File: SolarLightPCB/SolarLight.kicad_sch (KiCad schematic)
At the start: 20 parts, among them J1 I2C, J2 SPI, U1 TP4056, U2 WeMos_D1_mini, U3 MCP1700-3302E

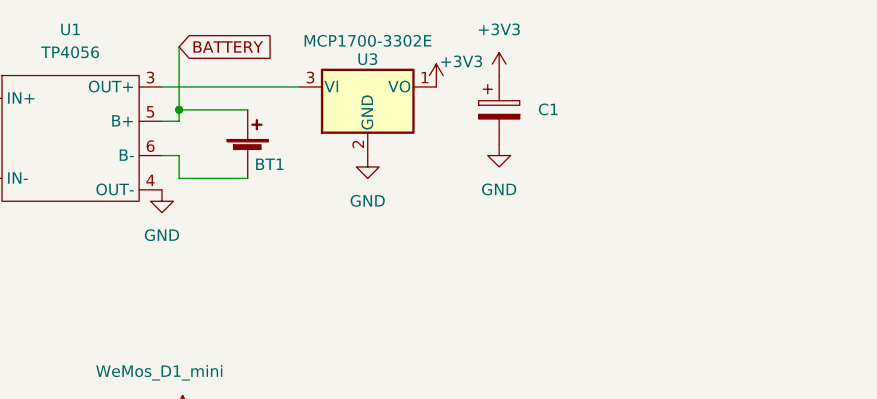
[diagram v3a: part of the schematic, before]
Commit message: Add a power on Jumper
fixes #5
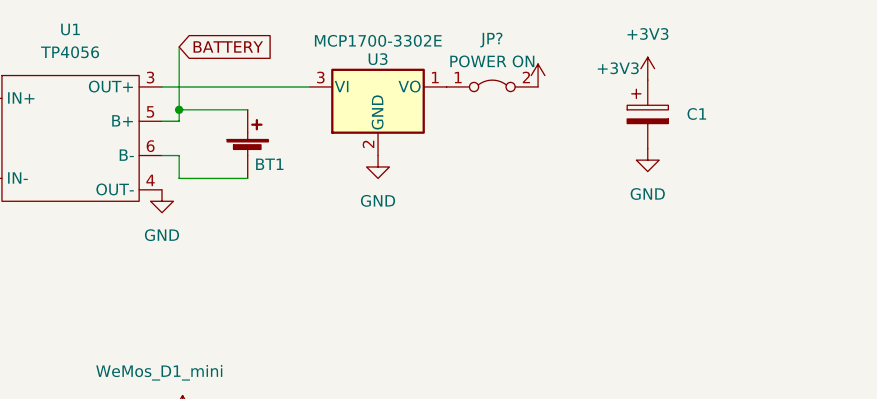
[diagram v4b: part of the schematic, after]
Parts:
- added JP?: POWER ON, Connector_PinHeader_2.54mm:PinHeader_1x02_P2.54mm_Vertical, symbol Jumper:Jumper_2_Bridged
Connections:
- net +3V3: now also JP?.2 (B); no longer U3.1 (VO)
- new net: JP?.1 (A), U3.1 (VO)
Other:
- moved on the sheet: C1, U3
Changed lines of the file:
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@@
     (stroke (width 0) (type default) (color 0 0 0 0))
   )
-  (wire (pts (xy 138.811 39.624) (xy 154.051 39.624))
+  (wire (pts (xy 138.811 39.624) (xy 155.194 39.624))
     (stroke (width 0) (type default) (color 0 0 0 0))
   )
@@
     (pin "2")
   )
-  (symbol (lib_id "power:GND") (at 176.276 45.974 0) (unit 1)
-    (in_bom yes) (on_board yes) (fields_autoplaced)
-    (property "Reference" "#PWR0103" (id 0) (at 176.276 52.324 0)
-      (effects (font (size 1.27 1.27)) hide)
-    )
-    (property "Value" "GND" (id 1) (at 176.276 51.054 0))
-    (property "Footprint" "" (id 2) (at 176.276 45.974 0)
-      (effects (font (size 1.27 1.27)) hide)
-    )
-    (property "Datasheet" "" (id 3) (at 176.276 45.974 0)
+  (symbol (lib_id "power:GND") (at 192.786 46.482 0) (unit 1)
+    (in_bom yes) (on_board yes) (fields_autoplaced)
+    (property "Reference" "#PWR0103" (id 0) (at 192.786 52.832 0)
+      (effects (font (size 1.27 1.27)) hide)
+    )
+    (property "Value" "GND" (id 1) (at 192.786 51.562 0))
+    (property "Footprint" "" (id 2) (at 192.786 46.482 0)
+      (effects (font (size 1.27 1.27)) hide)
+    )
+    (property "Datasheet" "" (id 3) (at 192.786 46.482 0)
       (effects (font (size 1.27 1.27)) hide)
     )
@@
     (pin "1")
   )
-  (symbol (lib_id "power:+3V3") (at 169.291 39.624 0) (unit 1)
-    (in_bom yes) (on_board yes)
-    (property "Reference" "#PWR0104" (id 0) (at 169.291 43.434 0)
-      (effects (font (size 1.27 1.27)) hide)
-    )
-    (property "Value" "+3V3" (id 1) (at 172.085 36.83 0))
-    (property "Footprint" "" (id 2) (at 169.291 39.624 0)
-      (effects (font (size 1.27 1.27)) hide)
-    )
-    (property "Datasheet" "" (id 3) (at 169.291 39.624 0)
+  (symbol (lib_id "power:+3V3") (at 180.594 39.624 0) (unit 1)
+    (in_bom yes) (on_board yes)
+    (property "Reference" "#PWR0104" (id 0) (at 180.594 43.434 0)
+      (effects (font (size 1.27 1.27)) hide)
+    )
+    (property "Value" "+3V3" (id 1) (at 189.484 37.592 0))
+    (property "Footprint" "" (id 2) (at 180.594 39.624 0)
+      (effects (font (size 1.27 1.27)) hide)
+    )
+    (property "Datasheet" "" (id 3) (at 180.594 39.624 0)
       (effects (font (size 1.27 1.27)) hide)
     )
@@
     )
   )
-  (symbol (lib_id "Regulator_Linear:L78L33_TO92") (at 161.671 39.624 0) (unit 1)
-    (in_bom yes) (on_board yes)
-    (property "Reference" "U3" (id 0) (at 161.671 36.576 0))
-    (property "Value" "MCP1700-3302E" (id 1) (at 161.671 34.544 0))
-    (property "Footprint" "Package_TO_SOT_THT:TO-92_Inline" (id 2) (at 161.671 33.909 0)
+  (symbol (lib_id "Regulator_Linear:L78L33_TO92") (at 162.814 39.624 0) (unit 1)
+    (in_bom yes) (on_board yes)
+    (property "Reference" "U3" (id 0) (at 162.814 36.576 0))
+    (property "Value" "MCP1700-3302E" (id 1) (at 162.814 34.544 0))
+    (property "Footprint" "Package_TO_SOT_THT:TO-92_Inline" (id 2) (at 162.814 33.909 0)
       (effects (font (size 1.27 1.27) italic) hide)
     )
-    (property "Datasheet" "http://www.st.com/content/ccc/resource/technical/document/datasheet/15/55/e5/aa/23/5b/43/fd/CD00000446.pdf/files/CD00000446.pdf/jcr:content/translations/en.CD00000446.pdf" (id 3) (at 161.671 40.894 0)
+    (property "Datasheet" "http://www.st.com/content/ccc/resource/technical/document/datasheet/15/55/e5/aa/23/5b/43/fd/CD00000446.pdf/files/CD00000446.pdf/jcr:content/translations/en.CD00000446.pdf" (id 3) (at 162.814 40.894 0)
       (effects (font (size 1.27 1.27)) hide)
     )
@@
     (pin "2")
   )
-  (symbol (lib_id "power:+3V3") (at 176.276 38.354 0) (unit 1)
-    (in_bom yes) (on_board yes) (fields_autoplaced)
-    (property "Reference" "#PWR0105" (id 0) (at 176.276 42.164 0)
-      (effects (font (size 1.27 1.27)) hide)
-    )
-    (property "Value" "+3V3" (id 1) (at 176.276 33.274 0))
-    (property "Footprint" "" (id 2) (at 176.276 38.354 0)
-      (effects (font (size 1.27 1.27)) hide)
-    )
-    (property "Datasheet" "" (id 3) (at 176.276 38.354 0)
+  (symbol (lib_id "power:+3V3") (at 192.786 38.862 0) (unit 1)
+    (in_bom yes) (on_board yes) (fields_autoplaced)
+    (property "Reference" "#PWR0105" (id 0) (at 192.786 42.672 0)
+      (effects (font (size 1.27 1.27)) hide)
+    )
+    (property "Value" "+3V3" (id 1) (at 192.786 33.782 0))
+    (property "Footprint" "" (id 2) (at 192.786 38.862 0)
+      (effects (font (size 1.27 1.27)) hide)
+    )
+    (property "Datasheet" "" (id 3) (at 192.786 38.862 0)
       (effects (font (size 1.27 1.27)) hide)
     )
@@
     )
   )
+  (symbol (lib_id "Jumper:Jumper_2_Bridged") (at 175.514 39.624 0) (unit 1)
+    (in_bom yes) (on_board yes) (fields_autoplaced)
+    (property "Reference" "JP?" (id 0) (at 175.514 34.29 0))
+    (property "Value" "POWER ON" (id 1) (at 175.514 36.83 0))
+    (property "Footprint" "Connector_PinHeader_2.54mm:PinHeader_1x02_P2.54mm_Vertical" (id 2) (at 175.514 39.624 0)
+      (effects (font (size 1.27 1.27)) hide)
+    )
+    (property "Datasheet" "~" (id 3) (at 175.514 39.624 0)
+      (effects (font (size 1.27 1.27)) hide)
+    )
+    (pin "1")
+    (pin "2")
+  )
   (symbol (lib_id "Connector:Conn_01x04_Female") (at 190.119 83.947 0) (unit 1)
     (in_bom yes) (on_board yes) (fields_autoplaced)
@@
     (pin "4")
   )
-  (symbol (lib_id "power:GND") (at 161.671 47.244 0) (unit 1)
-    (in_bom yes) (on_board yes) (fields_autoplaced)
-    (property "Reference" "#PWR0102" (id 0) (at 161.671 53.594 0)
-      (effects (font (size 1.27 1.27)) hide)
-    )
-    (property "Value" "GND" (id 1) (at 161.671 52.324 0))
-    (property "Footprint" "" (id 2) (at 161.671 47.244 0)
-      (effects (font (size 1.27 1.27)) hide)
-    )
-    (property "Datasheet" "" (id 3) (at 161.671 47.244 0)
+  (symbol (lib_id "power:GND") (at 162.814 47.244 0) (unit 1)
+    (in_bom yes) (on_board yes) (fields_autoplaced)
+    (property "Reference" "#PWR0102" (id 0) (at 162.814 53.594 0)
+      (effects (font (size 1.27 1.27)) hide)
+    )
+    (property "Value" "GND" (id 1) (at 162.814 52.324 0))
+    (property "Footprint" "" (id 2) (at 162.814 47.244 0)
+      (effects (font (size 1.27 1.27)) hide)
+    )
+    (property "Datasheet" "" (id 3) (at 162.814 47.244 0)
       (effects (font (size 1.27 1.27)) hide)
     )
@@
     (pin "3")
   )
-  (symbol (lib_id "Device:C_Polarized") (at 176.276 42.164 0) (unit 1)
-    (in_bom yes) (on_board yes)
-    (property "Reference" "C1" (id 0) (at 180.594 42.164 0)
-      (effects (font (size 1.27 1.27)) (justify left))
-    )
-    (property "Value" "C_Polarized" (id 1) (at 180.086 42.5449 0)
-      (effects (font (size 1.27 1.27)) (justify left) hide)
-    )
-    (property "Footprint" "Capacitor_THT:CP_Radial_D5.0mm_P2.00mm" (id 2) (at 177.2412 45.974 0)
-      (effects (font (size 1.27 1.27)) hide)
-    )
-    (property "Datasheet" "~" (id 3) (at 176.276 42.164 0)
+  (symbol (lib_id "Device:C_Polarized") (at 192.786 42.672 0) (unit 1)
+    (in_bom yes) (on_board yes)
+    (property "Reference" "C1" (id 0) (at 197.104 42.672 0)
+      (effects (font (size 1.27 1.27)) (justify left))
+    )
+    (property "Value" "C_Polarized" (id 1) (at 196.596 43.0529 0)
+      (effects (font (size 1.27 1.27)) (justify left) hide)
+    )
+    (property "Footprint" "Capacitor_THT:CP_Radial_D5.0mm_P2.00mm" (id 2) (at 193.7512 46.482 0)
+      (effects (font (size 1.27 1.27)) hide)
+    )
+    (property "Datasheet" "~" (id 3) (at 192.786 42.672 0)
       (effects (font (size 1.27 1.27)) hide)
     )
@@
       (reference "JP2") (unit 1) (value "Bridge") (footprint "Resistor_THT:R_Box_L8.4mm_W2.5mm_P5.08mm")
     )
+    (path "/a7c8a88d-781a-4fef-ada5-cbae7e10a79c"
+      (reference "JP?") (unit 1) (value "POWER ON") (footprint "Connector_PinHeader_2.54mm:PinHeader_1x02_P2.54mm_Vertical")
+    )
     (path "/efe1edb9-34c9-473f-839b-20e06ddf294c"

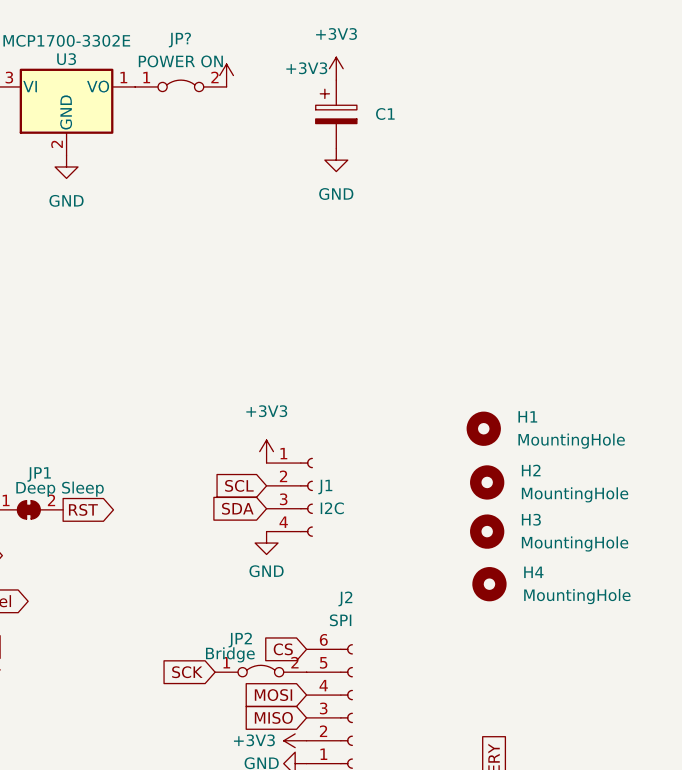
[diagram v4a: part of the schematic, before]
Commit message: Minor changes to PCB
- Added _draft_ mounting holes
- Added SPI and I2C labels
- Changed the Board dimension to 100x45mm
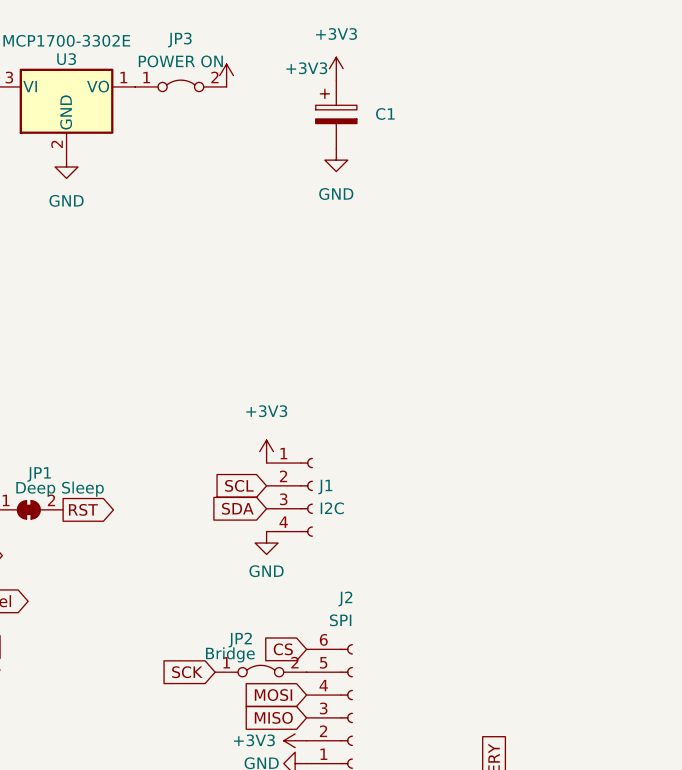
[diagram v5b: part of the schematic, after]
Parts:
- removed H1, H2, H3, H4: MountingHole, MountingHole:MountingHole_3.2mm_M3, symbol Mechanical:MountingHole
- U3: footprint Package_TO_SOT_THT:TO-92_Inline -> Package_TO_SOT_THT:TO-92
- gave numbers to parts that had none: 1
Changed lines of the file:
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@@
     (pin "1")
-  )
-  (symbol (lib_id "Mechanical:MountingHole") (at 209.169 77.597 0) (unit 1)
-    (in_bom yes) (on_board yes) (fields_autoplaced)
-    (property "Reference" "H1" (id 0) (at 212.852 76.3269 0)
-      (effects (font (size 1.27 1.27)) (justify left))
-    )
-    (property "Value" "MountingHole" (id 1) (at 212.852 78.8669 0)
-      (effects (font (size 1.27 1.27)) (justify left))
-    )
-    (property "Footprint" "MountingHole:MountingHole_3.2mm_M3" (id 2) (at 209.169 77.597 0)
-      (effects (font (size 1.27 1.27)) hide)
-    )
-    (property "Datasheet" "~" (id 3) (at 209.169 77.597 0)
-      (effects (font (size 1.27 1.27)) hide)
-    )
   )
   (symbol (lib_id "power:GND") (at 113.919 107.188 0) (unit 1)
@@
     (pin "1")
   )
-  (symbol (lib_id "Mechanical:MountingHole") (at 209.55 89.027 0) (unit 1)
-    (in_bom yes) (on_board yes) (fields_autoplaced)
-    (property "Reference" "H3" (id 0) (at 213.233 87.7569 0)
-      (effects (font (size 1.27 1.27)) (justify left))
-    )
-    (property "Value" "MountingHole" (id 1) (at 213.233 90.2969 0)
-      (effects (font (size 1.27 1.27)) (justify left))
-    )
-    (property "Footprint" "MountingHole:MountingHole_3.2mm_M3" (id 2) (at 209.55 89.027 0)
-      (effects (font (size 1.27 1.27)) hide)
-    )
-    (property "Datasheet" "~" (id 3) (at 209.55 89.027 0)
-      (effects (font (size 1.27 1.27)) hide)
-    )
-  )
   (symbol (lib_id "Regulator_Linear:L78L33_TO92") (at 162.814 39.624 0) (unit 1)
     (in_bom yes) (on_board yes)
     (property "Reference" "U3" (id 0) (at 162.814 36.576 0))
     (property "Value" "MCP1700-3302E" (id 1) (at 162.814 34.544 0))
-    (property "Footprint" "Package_TO_SOT_THT:TO-92_Inline" (id 2) (at 162.814 33.909 0)
+    (property "Footprint" "Package_TO_SOT_THT:TO-92" (id 2) (at 162.814 33.909 0)
       (effects (font (size 1.27 1.27) italic) hide)
     )
@@
     (pin "2")
   )
-  (symbol (lib_id "Mechanical:MountingHole") (at 209.55 83.566 0) (unit 1)
-    (in_bom yes) (on_board yes) (fields_autoplaced)
-    (property "Reference" "H2" (id 0) (at 213.233 82.2959 0)
-      (effects (font (size 1.27 1.27)) (justify left))
-    )
-    (property "Value" "MountingHole" (id 1) (at 213.233 84.8359 0)
-      (effects (font (size 1.27 1.27)) (justify left))
-    )
-    (property "Footprint" "MountingHole:MountingHole_3.2mm_M3" (id 2) (at 209.55 83.566 0)
-      (effects (font (size 1.27 1.27)) hide)
-    )
-    (property "Datasheet" "~" (id 3) (at 209.55 83.566 0)
-      (effects (font (size 1.27 1.27)) hide)
-    )
-  )
   (symbol (lib_id "Jumper:Jumper_2_Bridged") (at 175.514 39.624 0) (unit 1)
     (in_bom yes) (on_board yes) (fields_autoplaced)
-    (property "Reference" "JP?" (id 0) (at 175.514 34.29 0))
+    (property "Reference" "JP3" (id 0) (at 175.514 34.29 0))
     (property "Value" "POWER ON" (id 1) (at 175.514 36.83 0))
     (property "Footprint" "Connector_PinHeader_2.54mm:PinHeader_1x02_P2.54mm_Vertical" (id 2) (at 175.514 39.624 0)
@@
     (pin "3")
   )
-  (symbol (lib_id "Mechanical:MountingHole") (at 209.804 94.869 0) (unit 1)
-    (in_bom yes) (on_board yes) (fields_autoplaced)
-    (property "Reference" "H4" (id 0) (at 213.487 93.5989 0)
-      (effects (font (size 1.27 1.27)) (justify left))
-    )
-    (property "Value" "MountingHole" (id 1) (at 213.487 96.1389 0)
-      (effects (font (size 1.27 1.27)) (justify left))
-    )
-    (property "Footprint" "MountingHole:MountingHole_3.2mm_M3" (id 2) (at 209.804 94.869 0)
-      (effects (font (size 1.27 1.27)) hide)
-    )
-    (property "Datasheet" "~" (id 3) (at 209.804 94.869 0)
-      (effects (font (size 1.27 1.27)) hide)
-    )
-  )
   (symbol (lib_id "power:GND") (at 138.557 117.094 0) (unit 1)
     (in_bom yes) (on_board yes) (fields_autoplaced)
@@
       (reference "D1") (unit 1) (value "LED") (footprint "LED_THT:LED_D5.0mm")
     )
-    (path "/549ee4a0-6efe-4b7e-b8b9-e03448eeadd5"
-      (reference "H1") (unit 1) (value "MountingHole") (footprint "MountingHole:MountingHole_3.2mm_M3")
-    )
-    (path "/a26a0f96-4c32-40ac-a46d-b43387056357"
-      (reference "H2") (unit 1) (value "MountingHole") (footprint "MountingHole:MountingHole_3.2mm_M3")
-    )
-    (path "/65fee7b1-ae34-4d7e-a44d-061cf1cd3185"
-      (reference "H3") (unit 1) (value "MountingHole") (footprint "MountingHole:MountingHole_3.2mm_M3")
-    )
-    (path "/f8ae422c-f81f-4e3c-8596-a98120d415fe"
-      (reference "H4") (unit 1) (value "MountingHole") (footprint "MountingHole:MountingHole_3.2mm_M3")
-    )
     (path "/b014f64b-63d7-4679-a15c-8f4cf024b19d"
       (reference "J1") (unit 1) (value "I2C") (footprint "Connector_PinHeader_2.54mm:PinHeader_1x04_P2.54mm_Vertical")
@@
     )
     (path "/a7c8a88d-781a-4fef-ada5-cbae7e10a79c"
-      (reference "JP?") (unit 1) (value "POWER ON") (footprint "Connector_PinHeader_2.54mm:PinHeader_1x02_P2.54mm_Vertical")
+      (reference "JP3") (unit 1) (value "POWER ON") (footprint "Connector_PinHeader_2.54mm:PinHeader_1x02_P2.54mm_Vertical")
     )
     (path "/efe1edb9-34c9-473f-839b-20e06ddf294c"
@@
     )
     (path "/6732d4fc-02ff-4210-8868-4a455e8eb581"
-      (reference "U3") (unit 1) (value "MCP1700-3302E") (footprint "Package_TO_SOT_THT:TO-92_Inline")
-    )
-  )
+      (reference "U3") (unit 1) (value "MCP1700-3302E") (footprint "Package_TO_SOT_THT:TO-92")
+    )
+  )

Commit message: PCB Improvements
- Bigger Package for the voltage regulator
- Only one trace per pad (prefer to merge in the track instead)
- Specify some minimal trace distance
- Finer grid for the PCB to allow for better routing (5mils)
- Cleanup unconnected traces
- Ignore non-relevant DRC warnings
- Run DRC
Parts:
- U3: footprint Package_TO_SOT_THT:TO-92 -> Package_TO_SOT_THT:TO-92L_Wide
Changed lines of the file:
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@@
     (property "Reference" "U3" (id 0) (at 162.814 36.576 0))
     (property "Value" "MCP1700-3302E" (id 1) (at 162.814 34.544 0))
-    (property "Footprint" "Package_TO_SOT_THT:TO-92" (id 2) (at 162.814 33.909 0)
+    (property "Footprint" "Package_TO_SOT_THT:TO-92L_Wide" (id 2) (at 162.814 33.909 0)
       (effects (font (size 1.27 1.27) italic) hide)
     )
@@
     )
     (path "/6732d4fc-02ff-4210-8868-4a455e8eb581"
-      (reference "U3") (unit 1) (value "MCP1700-3302E") (footprint "Package_TO_SOT_THT:TO-92")
-    )
-  )
+      (reference "U3") (unit 1) (value "MCP1700-3302E") (footprint "Package_TO_SOT_THT:TO-92L_Wide")
+    )
+  )
